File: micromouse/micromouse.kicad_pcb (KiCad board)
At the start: 2 copper layers, 128.6 x 114.7 mm, 81 parts, among them IC1 STM32F205RET7, J1 B2B-PH-K-S, J2 B2B-PH-K-S, J3 Left Header, J4 Left Header, J5 Conn_01x04_Pin, Q1 ir_reciever, Q2 ir_reciever, Q3 SFH_313_FA-3_4, Q4 SFH_313_FA-3_4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

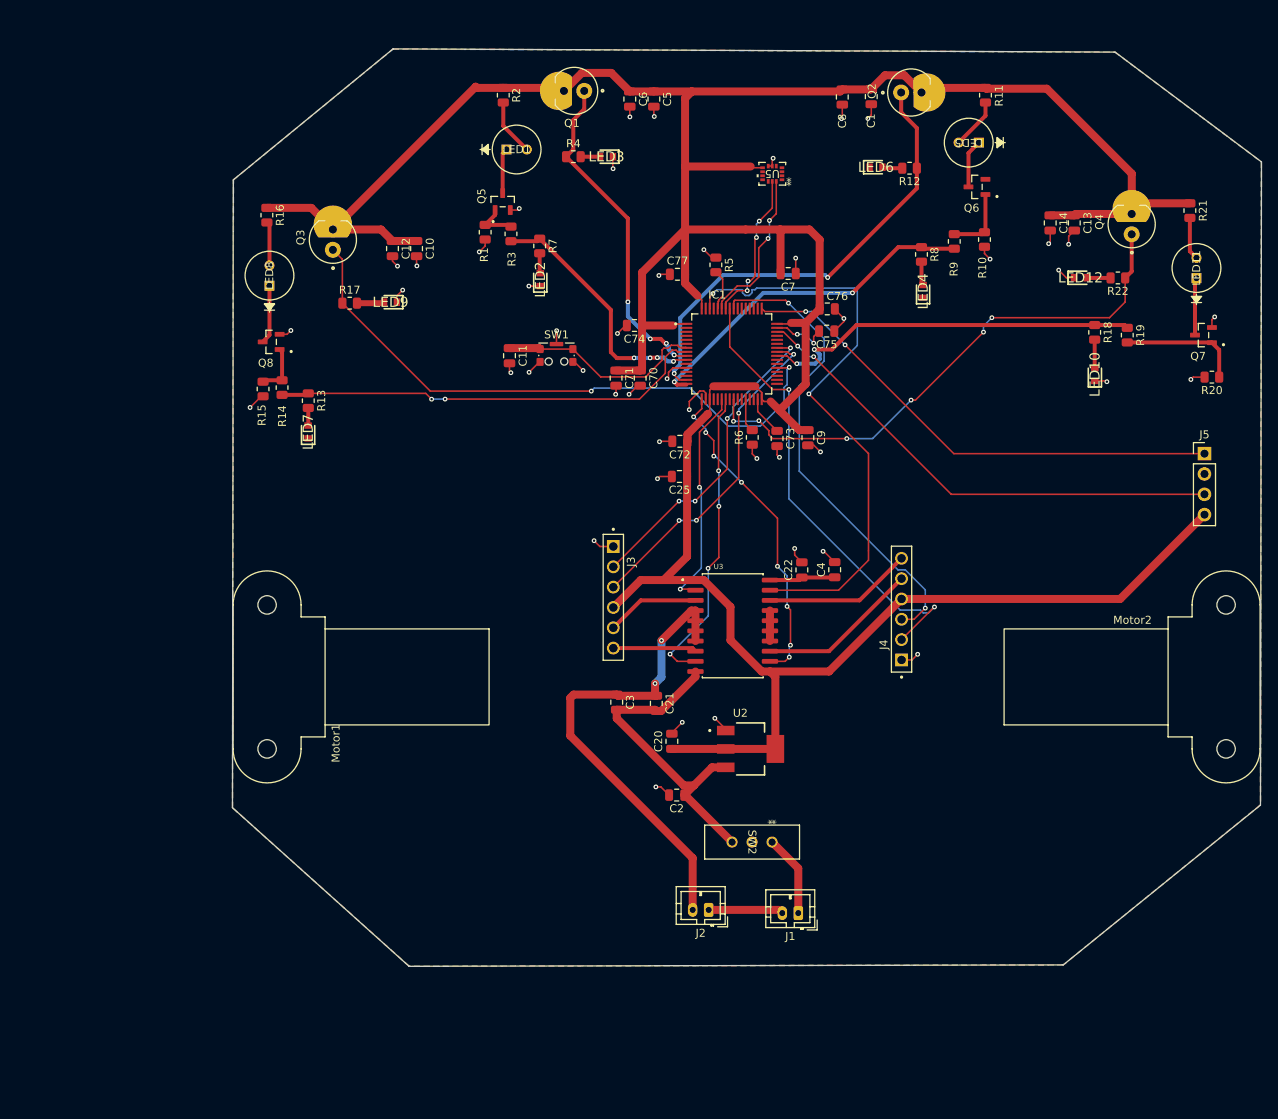
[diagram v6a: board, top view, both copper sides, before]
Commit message: PCB Change
routed MGND to GND
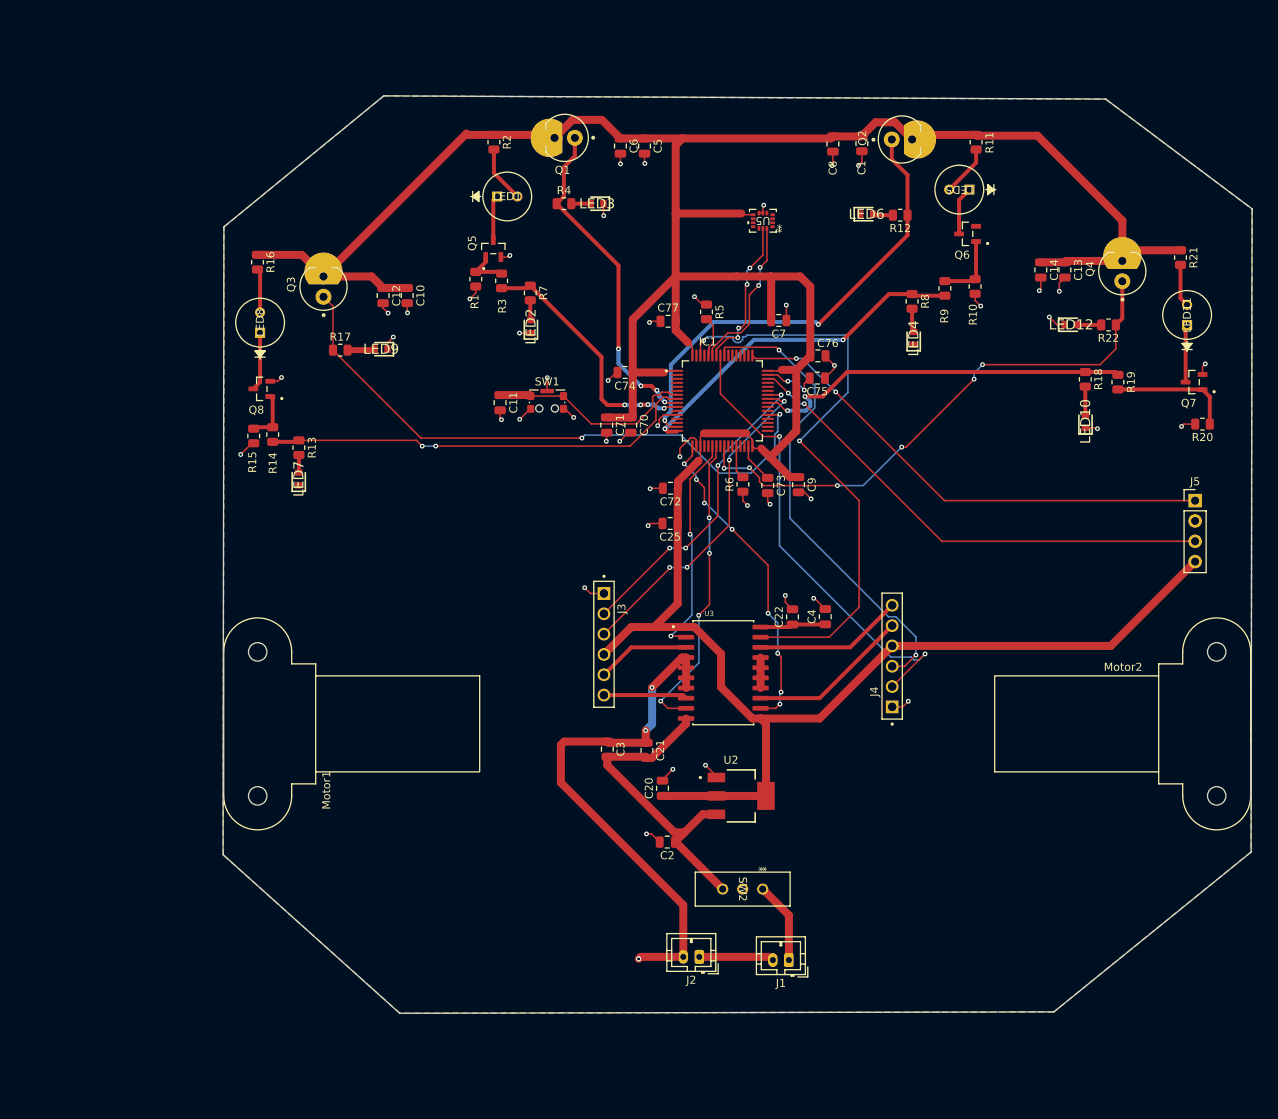
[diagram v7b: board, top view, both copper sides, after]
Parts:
- moved LED10 5.99 mm to (145.9, 57.3)
- moved Motor2 5.99 mm to (158.8, 96.6)
- moved Q4 5.99 mm to (150.5, 38.5)
- moved R1 5.99 mm to (69.6, 39.5)
- moved R18 5.99 mm to (145.8, 52.1)
- moved R20 5.99 mm to (160.5, 57.7)
- moved R21 5.99 mm to (157.7, 36.8)
- moved C10 5.99 mm to (61.1, 41.6)
- moved C12 5.99 mm to (58.1, 41.6)
- moved C20 5.99 mm to (93.0, 103.2)
- moved C21 5.99 mm to (91.0, 98.4)
- moved C22 5.99 mm to (109.2, 81.7)
- moved C25 5.99 mm to (93.9, 70.1)
- moved C3 5.99 mm to (86.1, 98.3)
- moved C4 5.99 mm to (113.3, 81.7)
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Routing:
- net MGND: track 64.6 -> 70.2 mm
- net GND: vias 46 -> 48

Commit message: pcb changes
final ver 1
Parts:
- moved LED7 7.27 mm to (54.6, 66.0)
- moved R13 7.12 mm to (54.6, 60.5)
- moved C8 2.24 mm to (112.0, 22.9)
- moved R14 1.76 mm to (46.0, 59.2)
- moved C14 1.67 mm to (138.6, 38.4)
- moved C5 1.65 mm to (92.4, 23.0)
- moved C10 1.64 mm to (62.7, 41.6)
- moved R1 1.40 mm to (69.7, 40.9)
- moved LED2 1.40 mm to (76.6, 46.9)
- moved R3 1.40 mm to (72.9, 41.1)
- moved R7 1.40 mm to (76.5, 42.7)
- moved Motor2 1.05 mm to (157.7, 96.6)
- moved Motor1 0.93 mm to (45.0, 93.3)
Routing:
- net 3V3: track 431.2 -> 434.5 mm
- net Net-(Q8-Pad1): track 6.42 -> 9.02 mm
- net PC0: track 54.7 -> 53.1 mm
- net Net-(LED7-A): track 2.21 -> 3.75 mm
- net PC2: track 31.6 -> 30.3 mm
- net Net-(Q5-Pad1): track 5.68 -> 7.05 mm
- net GND: track 87.0 -> 88.1 mm
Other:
- outline, holes or cut-outs redrawn
